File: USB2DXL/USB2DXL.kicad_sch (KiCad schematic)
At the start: 13 parts, among them J1 Conn_01x02, J2 USB_C_Receptacle_USB2.0_16P, U1 CH340E

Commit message: 仮
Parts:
- added C10: 47u, Capacitor_THT:CP_Radial_D5.0mm_P2.00mm, symbol Device:C_Polarized_Small
- added C4, C5, C7, C8, C9: 0.1u, Capacitor_SMD:C_0402_1005Metric, symbol Device:C_Small
- added C6: 0.33u, Capacitor_SMD:C_0603_1608Metric, symbol Device:C_Small
- added D3: Green, LED_SMD:LED_0805_2012Metric_Pad1.15x1.40mm_HandSolder, symbol Device:LED_Small
- added J3, J5: Conn_01x03, Connector_JST:JST_EH_B3B-EH-A_1x03_P2.50mm_Vertical, symbol Connector_Generic:Conn_01x03
- added J4, J6, J7: Conn_01x04, Connector_Molex:Molex_SPOX_5267-04A_1x04_P2.50mm_Vertical, symbol Connector_Generic:Conn_01x04
- added R10, R7, R8: 10, Resistor_SMD:R_0402_1005Metric, symbol Device:R_Small
- added R11: 220k, Resistor_SMD:R_0402_1005Metric, symbol Device:R_Small
- added R12, R14: 10k, Resistor_SMD:R_0402_1005Metric, symbol Device:R_Small
- added R13: 10k, Capacitor_SMD:C_0402_1005Metric, symbol Device:R_Small
- added R5, R6: 4k7, Resistor_SMD:R_0402_1005Metric, symbol Device:R_Small
- added R9: 150, Resistor_SMD:R_0402_1005Metric, symbol Device:R_Small
- added U2: ISO7741DWR, ISO7741DWR:SOIC127P1030X265-16N, symbol ISO7741DWR:ISO7741DWR
- added U3: 78L05G-AB3-R, Package_TO_SOT_SMD:SOT-89-3, symbol ProLib_pcs_2025-07-07:78L05G-AB3-R
- added U4: SP485EEN-L/TR, SP485EEN-L/TR:NSOIC-8, symbol SP485EEN-L/TR:SP485EEN-L_TR
- added U5: TC7WH241FK, Package_SO:MSOP-8_3x3mm_P0.65mm, symbol MyLibrary:TC7WH241FK
- added U6: 74AHC1G08, Package_TO_SOT_SMD:SOT-23-5_HandSoldering, symbol 74xGxx:74AHC1G08
- C1: value 10u -> 4n7; footprint (none) -> Capacitor_SMD:C_0402_1005Metric
- C2, C3: footprint (none) -> Capacitor_SMD:C_0402_1005Metric
- D1, D2: footprint (none) -> LED_SMD:LED_0603_1608Metric
- J1: value Conn_01x02 -> XT60
- R1, R2, R4: footprint (none) -> Resistor_SMD:R_0402_1005Metric
- R3: value 5k -> 4k7; footprint (none) -> Resistor_SMD:R_0402_1005Metric
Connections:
- net +12V: now also C10.1, C6.1, J3.2 (Pin_2), J4.2 (Pin_2), J5.2 (Pin_2), J6.2 (Pin_2), J7.2 (Pin_2), R14.1, U3.3 (IN)
- net +5V: now also C4.1, R5.1, U2.1 (VCC1)
- net GND: now also C4.2, U2.2 (GND1), U2.8 (GND1-1)
- net GNDPWR: now also C10.2, C5.2, C6.2, C7.2, C8.2, C9.2, D3.1 (K), J3.1 (Pin_1), J4.1 (Pin_1), J5.1 (Pin_1), J6.1 (Pin_1), J7.1 (Pin_1), U2.15 (GND2-1), U2.9 (GND2), U3.2 (GND), U4.5 (GND), U5.4 (GND), U6.3 (GND)
- net RXD: now also U2.6 (OUTD)
- net TXD: now also U2.3 (INA)
- net TXDEN renamed TXNOW
- net TXNOW: now also U2.4 (INB)
- new net: R13.1, U5.6 (Y1), U6.2
- new net: R12.1, U4.1 (RO), U6.1
- new net: R8.1, U4.6 (A)
- new net: R7.1, U4.7 (B)
- new net: R10.1, R11.1, U5.2 (A1), U5.3 (Y2)
- new net: R5.2, U2.7 (EN1)
- new net: D3.2 (A), R14.2
- new net: R6.1, U2.10 (EN2)
- new net +5VP: C5.1, C7.1, C8.1, C9.1, R11.2, R12.2, R13.2, R6.2, U2.16 (VCC2), U3.1 (OUT), U4.8 (VCC), U5.8 (V_{cc}), U6.5 (VCC)
- new net A: J4.3 (Pin_3), J6.3 (Pin_3), J7.3 (Pin_3), R8.2, R9.1
- new net B: J4.4 (Pin_4), J6.4 (Pin_4), J7.4 (Pin_4), R7.2, R9.2
- new net DATA: J3.3 (Pin_3), J5.3 (Pin_3), R10.2
- new net RX: U2.11 (IND), U6.4
- new net TX: U2.14 (OUTA), U4.4 (DI), U5.5 (A2)
- new net TXEN: U2.13 (OUTB), U4.2 (*RE), U4.3 (DE), U5.1 (G^{-}), U5.7 (G)
- no-connect marks 4 -> 6
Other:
- moved on the sheet: J1

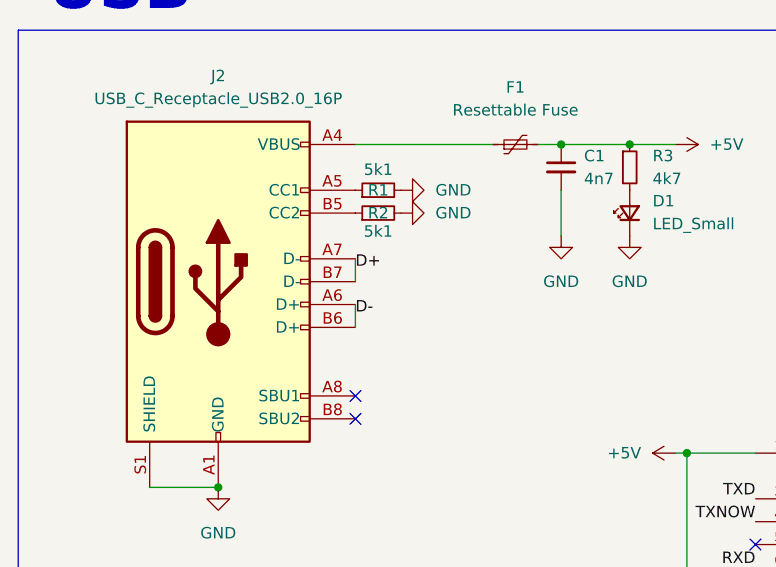
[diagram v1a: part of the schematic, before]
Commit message: D+とD-逆だったちね
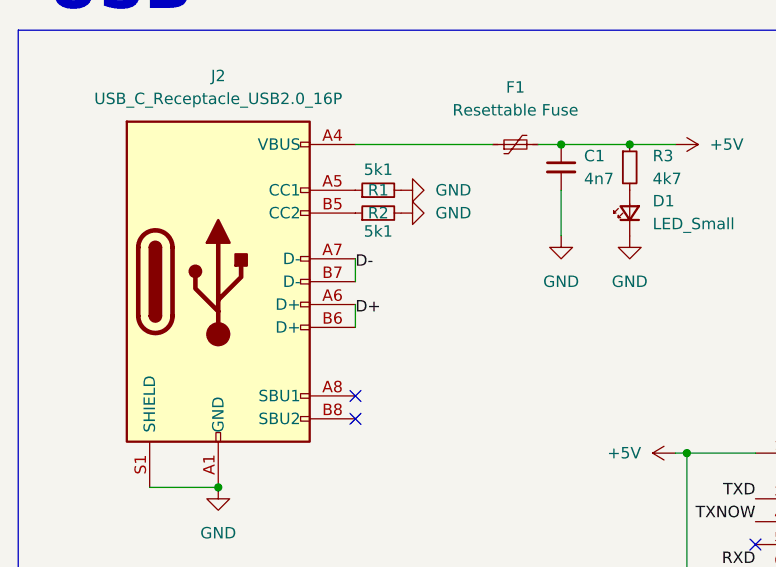
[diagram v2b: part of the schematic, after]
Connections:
- net D+: now also J2.A6 (D+), J2.B6 (D+); no longer J2.A7 (D-), J2.B7 (D-)
- net D-: now also J2.A7 (D-), J2.B7 (D-); no longer J2.A6 (D+), J2.B6 (D+)
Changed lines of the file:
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@@
-		)
-	)
-	(label "D-"
-		(at 60.96 69.85 0)
-		(effects
-			(font
-				(size 1.27 1.27)
-			)
-			(justify left bottom)
 		)
 	)
@@
 	)
 	(label "D-"
+		(at 60.96 64.77 0)
+		(effects
+			(font
+				(size 1.27 1.27)
+			)
+			(justify left bottom)
+		)
+	)
+	(label "D-"
 		(at 33.02 124.46 180)
 		(effects
@@
 		)
 	)
-	(label "D+"
-		(at 60.96 64.77 0)
-		(effects
-			(font
-				(size 1.27 1.27)
-			)
-			(justify left bottom)
-		)
-	)
 	(label "DATA-"
 		(at 214.63 153.67 180)
@@
 		)
 	)
+	(label "D+"
+		(at 60.96 69.85 0)
+		(effects
+			(font
+				(size 1.27 1.27)
+			)
+			(justify left bottom)
+		)
+	)

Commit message: マイコンからのUARTで動かせるようにした
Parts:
- removed F1: Resettable Fuse, Fuse:Fuse_0805_2012Metric_Pad1.15x1.40mm_HandSolder, symbol Device:Polyfuse_Small
- added R15: 10k, Resistor_SMD:R_0402_1005Metric, symbol Device:R_Small
- added U7: 74AHC1G08, Package_TO_SOT_SMD:SOT-23-5_HandSoldering, symbol 74xGxx:74AHC1G08
- J4: footprint Connector_Molex:Molex_SPOX_5267-04A_1x04_P2.50mm_Vertical -> Connector_JST:JST_XA_B04B-XASK-1_1x04_P2.50mm_Vertical
- R4: value 470 -> 1k
- U5: footprint Package_SO:MSOP-8_3x3mm_P0.65mm -> Package_SO:VSSOP-8_2.3x2mm_P0.5mm
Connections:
- net +12V: now also J6.3 (Pin_3), J7.3 (Pin_3); no longer J4.2 (Pin_2), J6.2 (Pin_2), J7.2 (Pin_2)
- net +5V: now also J2.A4 (VBUS), J2.A9 (VBUS), J2.B4 (VBUS), J2.B9 (VBUS), J4.2 (Pin_2), R15.2, U7.5 (VCC)
- net GND: now also J4.1 (Pin_1), U7.3 (GND)
- net GNDPWR: now also J6.4 (Pin_4), J7.4 (Pin_4); no longer J4.1 (Pin_1), J6.1 (Pin_1), J7.1 (Pin_1)
- net RXD: now also J4.4 (Pin_4)
- net TXD: now also U7.4; no longer U1.8 (TXD)
- removed net A: J4.3 (Pin_3), J6.3 (Pin_3), J7.3 (Pin_3), R8.2, R9.1
- removed net B: J4.4 (Pin_4), J6.4 (Pin_4), J7.4 (Pin_4), R7.2, R9.2
- new net DATA+: J6.2 (Pin_2), J7.2 (Pin_2), R8.2, R9.1
- new net DATA-: J6.1 (Pin_1), J7.1 (Pin_1), R7.2, R9.2
- new net TX_pin: J4.3 (Pin_3), R15.1, U7.1
- new net TX_usb: U1.8 (TXD), U7.2
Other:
- moved on the sheet: C1, D1, R3
